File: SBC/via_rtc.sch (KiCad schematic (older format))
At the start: 2 parts, among them U4 DS1511Y+

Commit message: Preparation for Pluto v3.0
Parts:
- C5: footprint Capacitors_ThroughHole:C_Disc_D4.7mm_W2.5mm_P5.00mm -> Capacitor_THT:C_Disc_D4.7mm_W2.5mm_P5.00mm
- U4: footprint Housings_DIP:DIP-28_W15.24mm_Socket -> Package_DIP:DIP-28_W15.24mm_Socket; symbol saturn:DS1511Y+ -> pluto-rescue:DS1511Y+-saturn
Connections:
- net labels added: ~RTC
- net labels removed: ~7F8X
- wire segments 27 -> 29
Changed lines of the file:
@@
 EESchema Schematic File Version 4
 LIBS:pluto-cache
-EELAYER 29 0
+EELAYER 30 0
 EELAYER END
 $Descr A4 11693 8268
@@
 F 0 "C5" V 6750 3800 50  0000 L CNN
 F 1 "0.1uF" V 6425 3750 50  0000 L CNN
-F 2 "Capacitors_ThroughHole:C_Disc_D4.7mm_W2.5mm_P5.00mm" H 6613 3700 50  0001 C CNN
+F 2 "Capacitor_THT:C_Disc_D4.7mm_W2.5mm_P5.00mm" H 6613 3700 50  0001 C CNN
 F 3 "" H 6575 3850 50  0001 C CNN
 	1    6575 3850
@@
 ~MRD
 Text HLabel 4750 2875 0    60   Input ~ 0
-~7F8X
+~RTC
 Wire Wire Line
 	5075 2675 4750 2675
@@
 Wire Wire Line
 	6125 2275 6450 2275
-Wire Bus Line
-	6550 2175 6550 2875
 Wire Wire Line
 	5075 2275 4750 2275
-Wire Bus Line
-	4650 1300 4650 2575
-$Comp
-L saturn:DS1511Y+ U4
+$Comp
+L pluto-rescue:DS1511Y+-saturn U4
 U 1 1 58D61FB4
 P 5550 2850
@@
 F 0 "U4" H 5375 3575 60  0000 C CNN
 F 1 "DS1511Y+" V 5600 2850 60  0000 C CNN
-F 2 "Housings_DIP:DIP-28_W15.24mm_Socket" H 5300 3300 60  0001 C CNN
+F 2 "Package_DIP:DIP-28_W15.24mm_Socket" H 5300 3300 60  0001 C CNN
 F 3 "" H 5300 3300 60  0001 C CNN
 	1    5550 2850
@@
 	6125 3475 6250 3475
 Wire Wire Line
-	5500 3850 6425 3850
+	5500 3850 5625 3850
 Connection ~ 5625 3850
 Text HLabel 6450 3225 2    60   Input ~ 0
@@
 Wire Bus Line
 	4650 1300 7375 1300
+Wire Wire Line
+	5625 3850 6250 3850
+Wire Wire Line
+	6250 3850 6425 3850
+Wire Bus Line
+	4650 1300 4650 2575
+Wire Bus Line
+	6550 2175 6550 2875
 $EndSCHEMATC

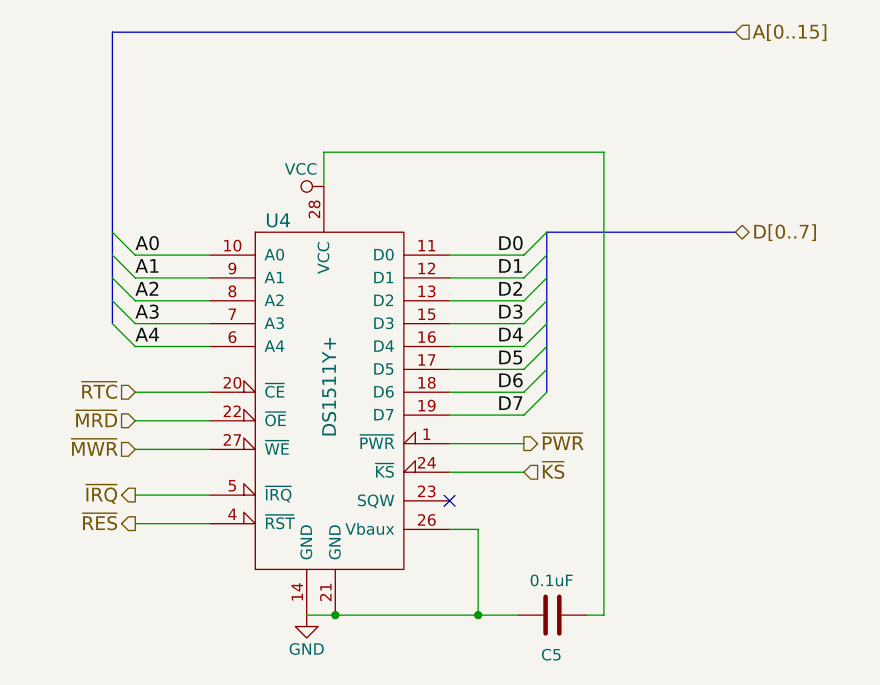
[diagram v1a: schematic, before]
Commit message: A better layout of PCB.
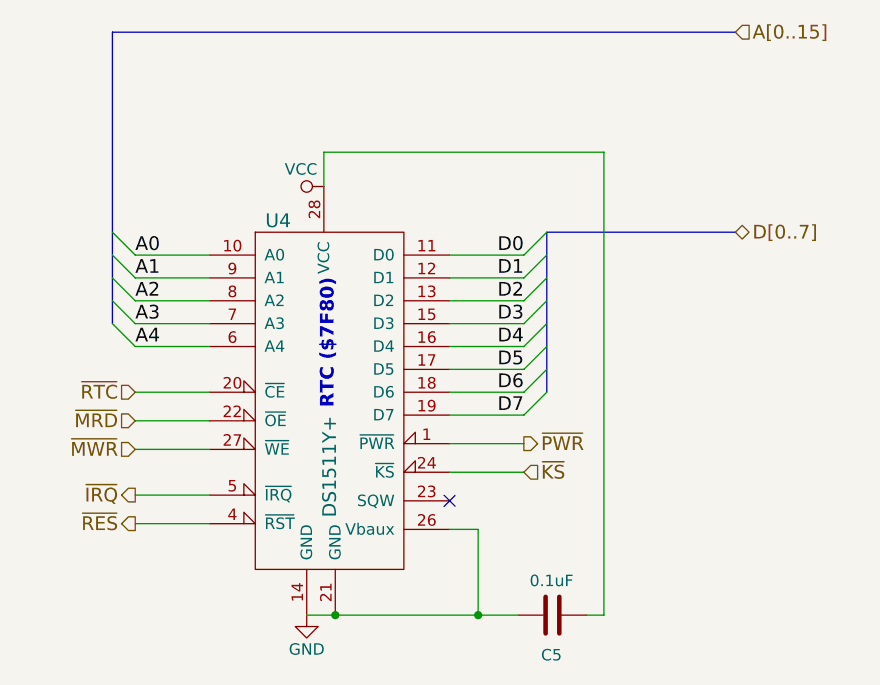
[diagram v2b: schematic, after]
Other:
- note added: "RTC ($7F80)"
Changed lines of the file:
@@
 AR Path="/58D58980/58D61FB4" Ref="U4"  Part="1"
 F 0 "U4" H 5375 3575 60  0000 C CNN
-F 1 "DS1511Y+" V 5600 2850 60  0000 C CNN
+F 1 "DS1511Y+" V 5600 2500 60  0000 C CNN
 F 2 "Package_DIP:DIP-28_W15.24mm_Socket" H 5300 3300 60  0001 C CNN
 F 3 "" H 5300 3300 60  0001 C CNN
@@
 Wire Bus Line
 	6550 2175 6550 2875
+Text Notes 5625 2950 1    60   ~ 12
+RTC ($7F80)
 $EndSCHEMATC

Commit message: Converting to SMD of almost all components.
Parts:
- C5: footprint Capacitor_THT:C_Disc_D4.7mm_W2.5mm_P5.00mm -> Capacitor_SMD:C_0603_1608Metric_Pad1.05x0.95mm_HandSolder
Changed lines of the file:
@@
 F 0 "C5" V 6750 3800 50  0000 L CNN
 F 1 "0.1uF" V 6425 3750 50  0000 L CNN
-F 2 "Capacitor_THT:C_Disc_D4.7mm_W2.5mm_P5.00mm" H 6613 3700 50  0001 C CNN
+F 2 "Capacitor_SMD:C_0603_1608Metric_Pad1.05x0.95mm_HandSolder" H 6613 3700 50  0001 C CNN
 F 3 "" H 6575 3850 50  0001 C CNN
 	1    6575 3850
@@
 Wire Wire Line
 	6250 3850 6425 3850
+Text Notes 5625 2950 1    60   ~ 12
+RTC ($7F80)
 Wire Bus Line
 	4650 1300 4650 2575
 Wire Bus Line
 	6550 2175 6550 2875
-Text Notes 5625 2950 1    60   ~ 12
-RTC ($7F80)
 $EndSCHEMATC

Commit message: New PCB layout is taking shape.
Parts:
- C5: footprint Capacitor_SMD:C_0603_1608Metric_Pad1.05x0.95mm_HandSolder -> Capacitor_SMD:C_0805_2012Metric_Pad1.15x1.40mm_HandSolder
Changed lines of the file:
@@
 F 0 "C5" V 6750 3800 50  0000 L CNN
 F 1 "0.1uF" V 6425 3750 50  0000 L CNN
-F 2 "Capacitor_SMD:C_0603_1608Metric_Pad1.05x0.95mm_HandSolder" H 6613 3700 50  0001 C CNN
+F 2 "Capacitor_SMD:C_0805_2012Metric_Pad1.15x1.40mm_HandSolder" H 6613 3700 50  0001 C CNN
 F 3 "" H 6575 3850 50  0001 C CNN
 	1    6575 3850
